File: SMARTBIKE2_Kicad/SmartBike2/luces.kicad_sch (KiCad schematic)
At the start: 5 parts, among them Q1 FDN340P, Q2 SI2302

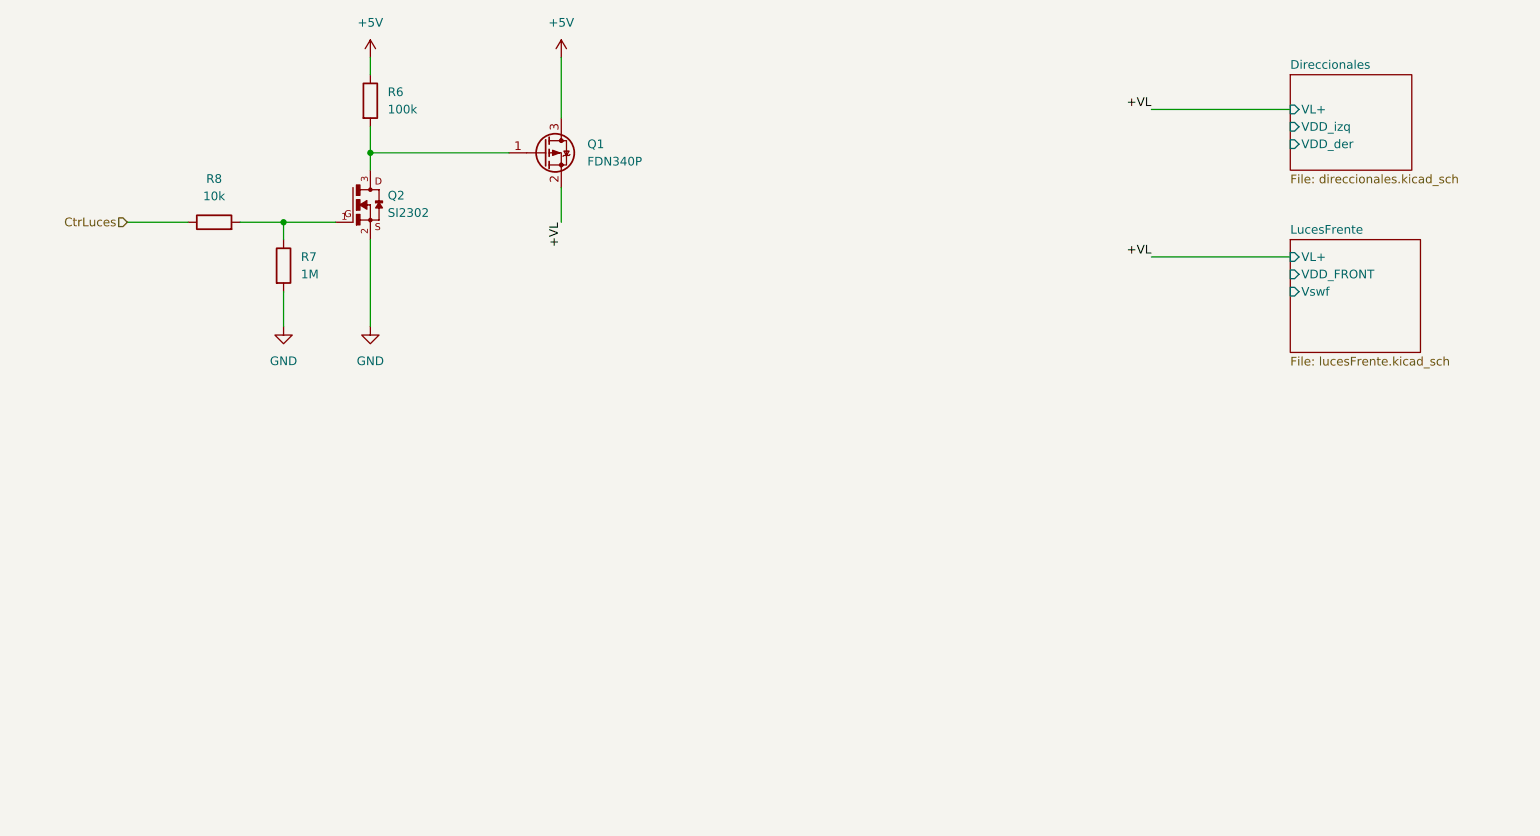
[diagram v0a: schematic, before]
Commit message: Alarma, luces frontales y modulos
+ Circuito luces frontales
+ Conector Luces
+ Conector GPS
+ Conector SIM
+ Conector acelerómetro

~ Acondicionamiento ESP32
~ Huellas
~ PCB
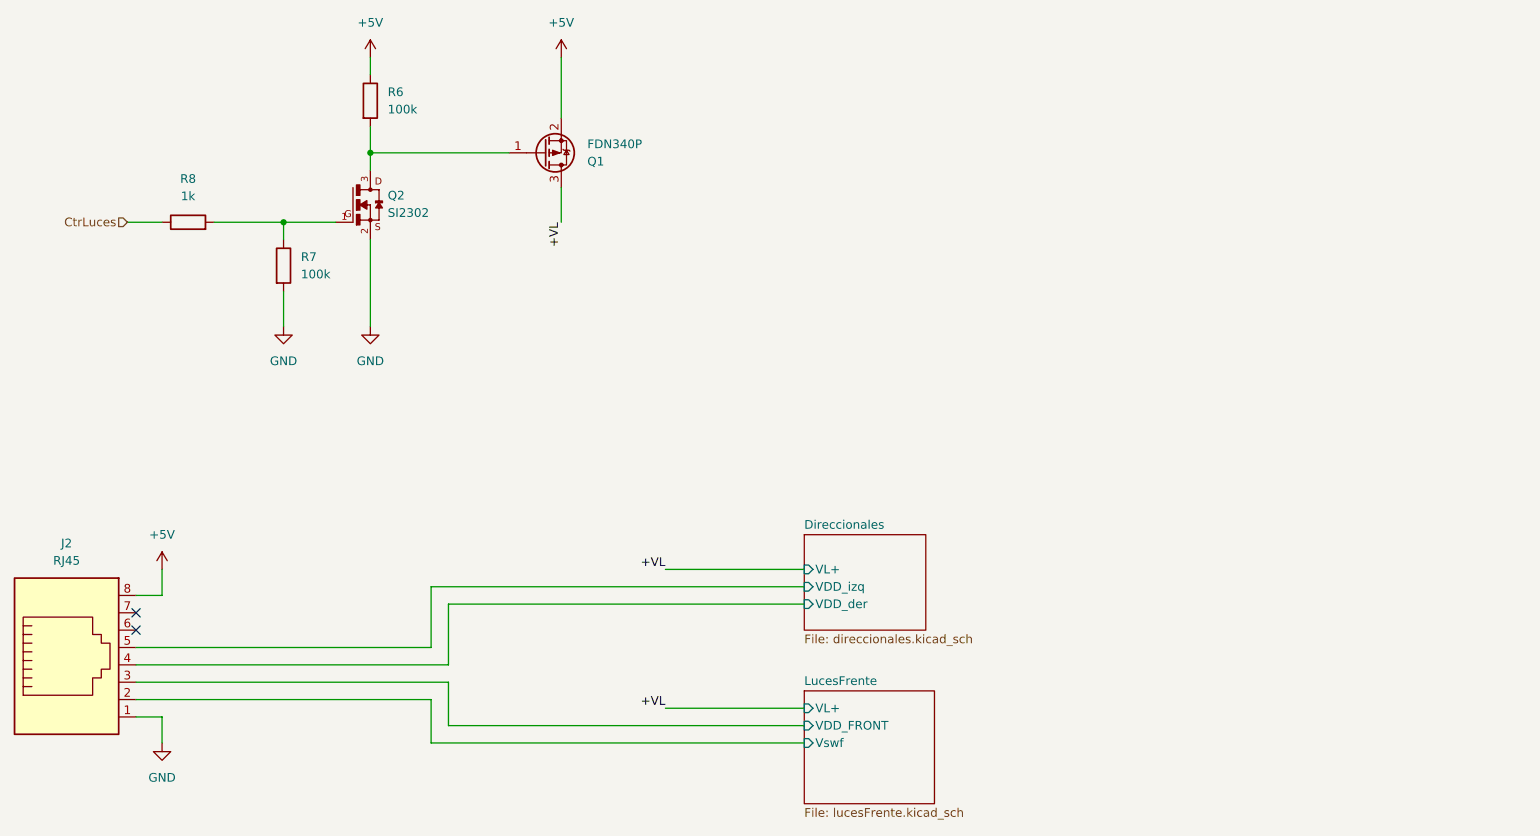
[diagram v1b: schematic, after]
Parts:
- added J2: RJ45, symbol Connector:RJ45
- R7: value 1M -> 100k
- R8: value 10k -> 1k
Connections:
- net +5V: now also Q1.2 (S), J2.8; no longer Q1.3 (D)
- net +VL: now also Q1.3 (D); no longer Q1.2 (S)
- net Direccionales/VDD_der: now also J2.4
- net Direccionales/VDD_izq: now also J2.5
- net GND: now also J2.1
- net LucesFrente/VDD_FRONT: now also J2.3
- net LucesFrente/Vswf: now also J2.2
- no-connect marks 0 -> 2
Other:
- moved on the sheet: R8

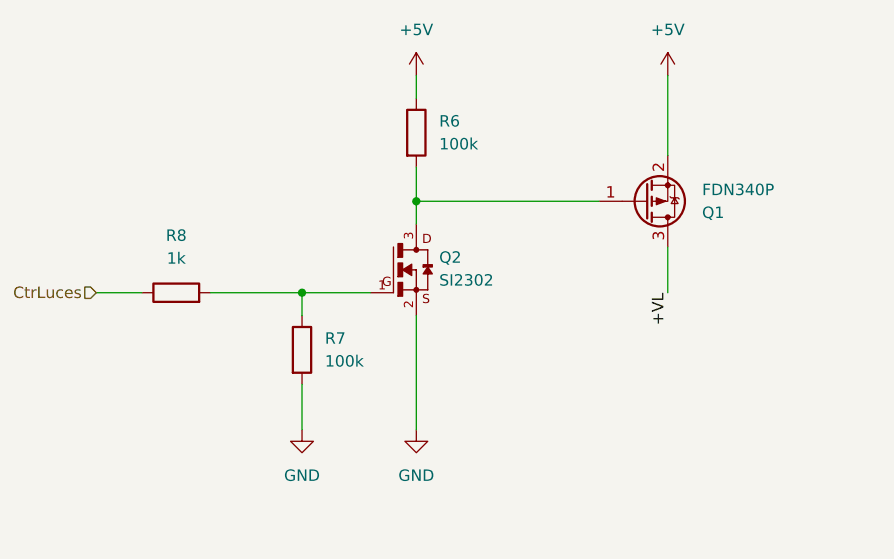
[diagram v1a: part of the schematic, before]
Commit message: Beta 100% esquemáticos
+ Acondicionamiento ESP32

~ Huellas
~ PCB
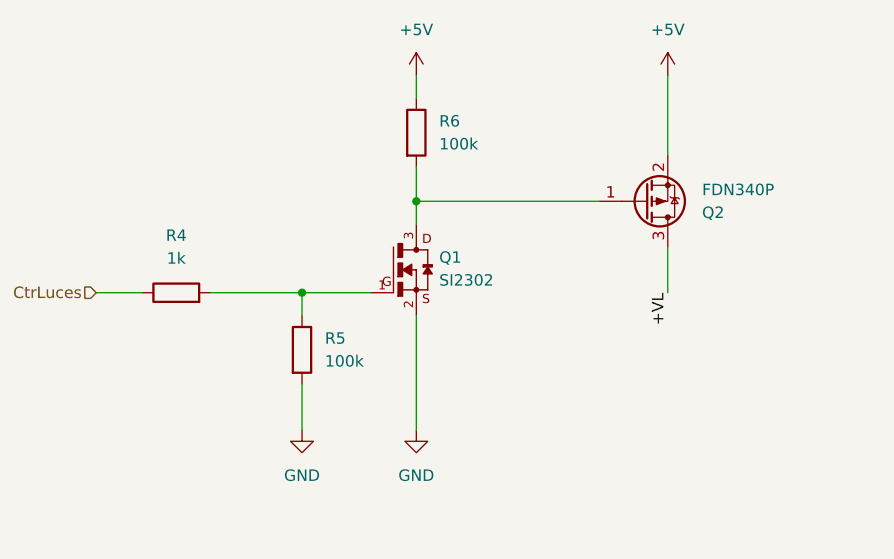
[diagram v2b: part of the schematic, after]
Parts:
- renumbered Q2 to Q1, Q1 to Q2, R8 to R4, R7 to R5
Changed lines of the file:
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@@
   (symbol (lib_id "power:GND") (at 76.2 69.85 0) (unit 1)
     (in_bom yes) (on_board yes) (dnp no) (fields_autoplaced)
-    (property "Reference" "#PWR09" (at 76.2 76.2 0)
+    (property "Reference" "#PWR011" (at 76.2 76.2 0)
       (effects (font (size 1.27 1.27)) hide)
     )
@@
       (project "SmartBike2"
         (path "/ec60d9f0-678c-40dc-aaf4-e99b29a92238/524d1916-2b88-4ec8-8df8-acd48937d478"
-          (reference "#PWR09") (unit 1)
+          (reference "#PWR011") (unit 1)
         )
       )
@@
   (symbol (lib_id "power:+5V") (at 88.9 30.48 0) (unit 1)
     (in_bom yes) (on_board yes) (dnp no) (fields_autoplaced)
-    (property "Reference" "#PWR07" (at 88.9 34.29 0)
+    (property "Reference" "#PWR012" (at 88.9 34.29 0)
       (effects (font (size 1.27 1.27)) hide)
     )
@@
       (project "SmartBike2"
         (path "/ec60d9f0-678c-40dc-aaf4-e99b29a92238/524d1916-2b88-4ec8-8df8-acd48937d478"
-          (reference "#PWR07") (unit 1)
+          (reference "#PWR012") (unit 1)
         )
       )
@@
   (symbol (lib_id "Transistor_FET:FDN340P") (at 114.3 44.45 0) (mirror x) (unit 1)
     (in_bom yes) (on_board yes) (dnp no)
-    (property "Reference" "Q1" (at 120.65 45.72 0)
+    (property "Reference" "Q2" (at 120.65 45.72 0)
       (effects (font (size 1.27 1.27)) (justify left))
     )
@@
       (project "SmartBike2"
         (path "/ec60d9f0-678c-40dc-aaf4-e99b29a92238/524d1916-2b88-4ec8-8df8-acd48937d478"
-          (reference "Q1") (unit 1)
+          (reference "Q2") (unit 1)
         )
       )
@@
   (symbol (lib_id "Device:R") (at 76.2 60.96 0) (unit 1)
     (in_bom yes) (on_board yes) (dnp no) (fields_autoplaced)
-    (property "Reference" "R7" (at 78.74 59.69 0)
+    (property "Reference" "R5" (at 78.74 59.69 0)
       (effects (font (size 1.27 1.27)) (justify left))
     )
@@
       (project "SmartBike2"
         (path "/ec60d9f0-678c-40dc-aaf4-e99b29a92238/524d1916-2b88-4ec8-8df8-acd48937d478"
-          (reference "R7") (unit 1)
+          (reference "R5") (unit 1)
         )
       )
@@
   (symbol (lib_id "Device:R") (at 62.23 54.61 90) (unit 1)
     (in_bom yes) (on_board yes) (dnp no) (fields_autoplaced)
-    (property "Reference" "R8" (at 62.23 48.26 90)
+    (property "Reference" "R4" (at 62.23 48.26 90)
       (effects (font (size 1.27 1.27)))
     )
@@
       (project "SmartBike2"
         (path "/ec60d9f0-678c-40dc-aaf4-e99b29a92238/524d1916-2b88-4ec8-8df8-acd48937d478"
-          (reference "R8") (unit 1)
+          (reference "R4") (unit 1)
         )
       )
@@
   (symbol (lib_id "power:+5V") (at 116.84 30.48 0) (unit 1)
     (in_bom yes) (on_board yes) (dnp no) (fields_autoplaced)
-    (property "Reference" "#PWR08" (at 116.84 34.29 0)
+    (property "Reference" "#PWR014" (at 116.84 34.29 0)
       (effects (font (size 1.27 1.27)) hide)
     )
@@
       (project "SmartBike2"
         (path "/ec60d9f0-678c-40dc-aaf4-e99b29a92238/524d1916-2b88-4ec8-8df8-acd48937d478"
-          (reference "#PWR08") (unit 1)
+          (reference "#PWR014") (unit 1)
         )
       )
@@
   (symbol (lib_id "SI2302:SI2302") (at 88.9 52.07 0) (unit 1)
     (in_bom yes) (on_board yes) (dnp no) (fields_autoplaced)
-    (property "Reference" "Q2" (at 91.44 50.6951 0)
+    (property "Reference" "Q1" (at 91.44 50.6951 0)
       (effects (font (size 1.27 1.27)) (justify left))
     )
@@
       (project "SmartBike2"
         (path "/ec60d9f0-678c-40dc-aaf4-e99b29a92238/524d1916-2b88-4ec8-8df8-acd48937d478"
-          (reference "Q2") (unit 1)
+          (reference "Q1") (unit 1)
         )
       )
@@
   (symbol (lib_id "power:GND") (at 88.9 69.85 0) (unit 1)
     (in_bom yes) (on_board yes) (dnp no) (fields_autoplaced)
-    (property "Reference" "#PWR06" (at 88.9 76.2 0)
+    (property "Reference" "#PWR013" (at 88.9 76.2 0)
       (effects (font (size 1.27 1.27)) hide)
     )
@@
       (project "SmartBike2"
         (path "/ec60d9f0-678c-40dc-aaf4-e99b29a92238/524d1916-2b88-4ec8-8df8-acd48937d478"
-          (reference "#PWR06") (unit 1)
+          (reference "#PWR013") (unit 1)
         )
       )
@@
   (symbol (lib_id "power:GND") (at 58.42 130.81 0) (unit 1)
     (in_bom yes) (on_board yes) (dnp no) (fields_autoplaced)
-    (property "Reference" "#PWR035" (at 58.42 137.16 0)
+    (property "Reference" "#PWR010" (at 58.42 137.16 0)
       (effects (font (size 1.27 1.27)) hide)
     )
@@
       (project "SmartBike2"
         (path "/ec60d9f0-678c-40dc-aaf4-e99b29a92238/524d1916-2b88-4ec8-8df8-acd48937d478"
-          (reference "#PWR035") (unit 1)
+          (reference "#PWR010") (unit 1)
         )
       )
@@
   (symbol (lib_id "power:+5V") (at 58.42 105.41 0) (unit 1)
     (in_bom yes) (on_board yes) (dnp no) (fields_autoplaced)
-    (property "Reference" "#PWR034" (at 58.42 109.22 0)
+    (property "Reference" "#PWR09" (at 58.42 109.22 0)
       (effects (font (size 1.27 1.27)) hide)
     )
@@
       (project "SmartBike2"
         (path "/ec60d9f0-678c-40dc-aaf4-e99b29a92238/524d1916-2b88-4ec8-8df8-acd48937d478"
-          (reference "#PWR034") (unit 1)
-        )
-      )
+          (reference "#PWR09") (unit 1)
+        )
+      )

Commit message: cache
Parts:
- Q1: footprint SI2302:SOT23 -> Package_TO_SOT_SMD:SOT-23
- Q2: footprint Package_TO_SOT_SMD:SOT-23 -> Package_TO_SOT_SMD:SuperSOT-3
- R4, R5, R6: footprint (none) -> Resistor_SMD:R_0805_2012Metric_Pad1.20x1.40mm_HandSolder
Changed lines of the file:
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@@
       (effects (font (size 1.27 1.27)) (justify left))
     )
-    (property "Footprint" "" (at 87.122 36.83 90)
+    (property "Footprint" "Resistor_SMD:R_0805_2012Metric_Pad1.20x1.40mm_HandSolder" (at 87.122 36.83 90)
       (effects (font (size 1.27 1.27)) hide)
     )
@@
       (effects (font (size 1.27 1.27)) (justify left))
     )
-    (property "Footprint" "Package_TO_SOT_SMD:SOT-23" (at 119.38 42.545 0)
+    (property "Footprint" "Package_TO_SOT_SMD:SuperSOT-3" (at 119.38 42.545 0)
       (effects (font (size 1.27 1.27) italic) (justify left) hide)
     )
@@
       (effects (font (size 1.27 1.27)) (justify left))
     )
-    (property "Footprint" "" (at 74.422 60.96 90)
+    (property "Footprint" "Resistor_SMD:R_0805_2012Metric_Pad1.20x1.40mm_HandSolder" (at 74.422 60.96 90)
       (effects (font (size 1.27 1.27)) hide)
     )
@@
       (effects (font (size 1.27 1.27)))
     )
-    (property "Footprint" "" (at 62.23 56.388 90)
+    (property "Footprint" "Resistor_SMD:R_0805_2012Metric_Pad1.20x1.40mm_HandSolder" (at 62.23 56.388 90)
       (effects (font (size 1.27 1.27)) hide)
     )
@@
       (effects (font (size 1.27 1.27)) (justify left))
     )
-    (property "Footprint" "SI2302:SOT23" (at 88.9 52.07 0)
+    (property "Footprint" "Package_TO_SOT_SMD:SOT-23" (at 88.9 52.07 0)
       (effects (font (size 1.27 1.27)) (justify bottom) hide)
     )

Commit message: mas huellas
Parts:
- J2: footprint (none) -> Connector_JST:JST_EH_B2B-EH-A_1x02_P2.50mm_Vertical
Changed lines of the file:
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@@
       (effects (font (size 1.27 1.27)))
     )
-    (property "Footprint" "" (at 44.45 118.745 90)
+    (property "Footprint" "Connector_JST:JST_EH_B2B-EH-A_1x02_P2.50mm_Vertical" (at 44.45 118.745 90)
       (effects (font (size 1.27 1.27)) hide)
     )

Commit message: Final Huellas
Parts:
- J2: footprint Connector_JST:JST_EH_B2B-EH-A_1x02_P2.50mm_Vertical -> Connector_RJ:RJ45_Amphenol_RJHSE538X
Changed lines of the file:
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@@
       (effects (font (size 1.27 1.27)))
     )
-    (property "Footprint" "Connector_JST:JST_EH_B2B-EH-A_1x02_P2.50mm_Vertical" (at 44.45 118.745 90)
+    (property "Footprint" "Connector_RJ:RJ45_Amphenol_RJHSE538X" (at 44.45 118.745 90)
       (effects (font (size 1.27 1.27)) hide)
     )
